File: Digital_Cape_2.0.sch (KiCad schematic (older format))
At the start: 15 parts, among them J1 RJ45, J2 RJ45, P8 BeagleBone_Black_Header, P9 BeagleBone_Black_Header

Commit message: Update of KiCad files
My apologies I'm still learning! Files from 02-13-2021 Hangar session
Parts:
- added H1, H2, H3, H4: MountingHole, MountingHole:MountingHole_3.2mm_M3, symbol Mechanical:MountingHole
- added R1, R2: 4.7k, Resistor_THT:R_Axial_DIN0204_L3.6mm_D1.6mm_P5.08mm_Horizontal, symbol Device:R
- C1, C2, C3, C4, C5, CP1, CP2: footprint Capacitor_SMD:CP_Elec_4x4.5 -> Capacitor_THT:C_Disc_D3.0mm_W2.0mm_P2.50mm
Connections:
- net labels removed: GND1, GND2, GNDA_ADC, GNDD
- wire segments 139 -> 164
- no-connect marks 78 -> 76

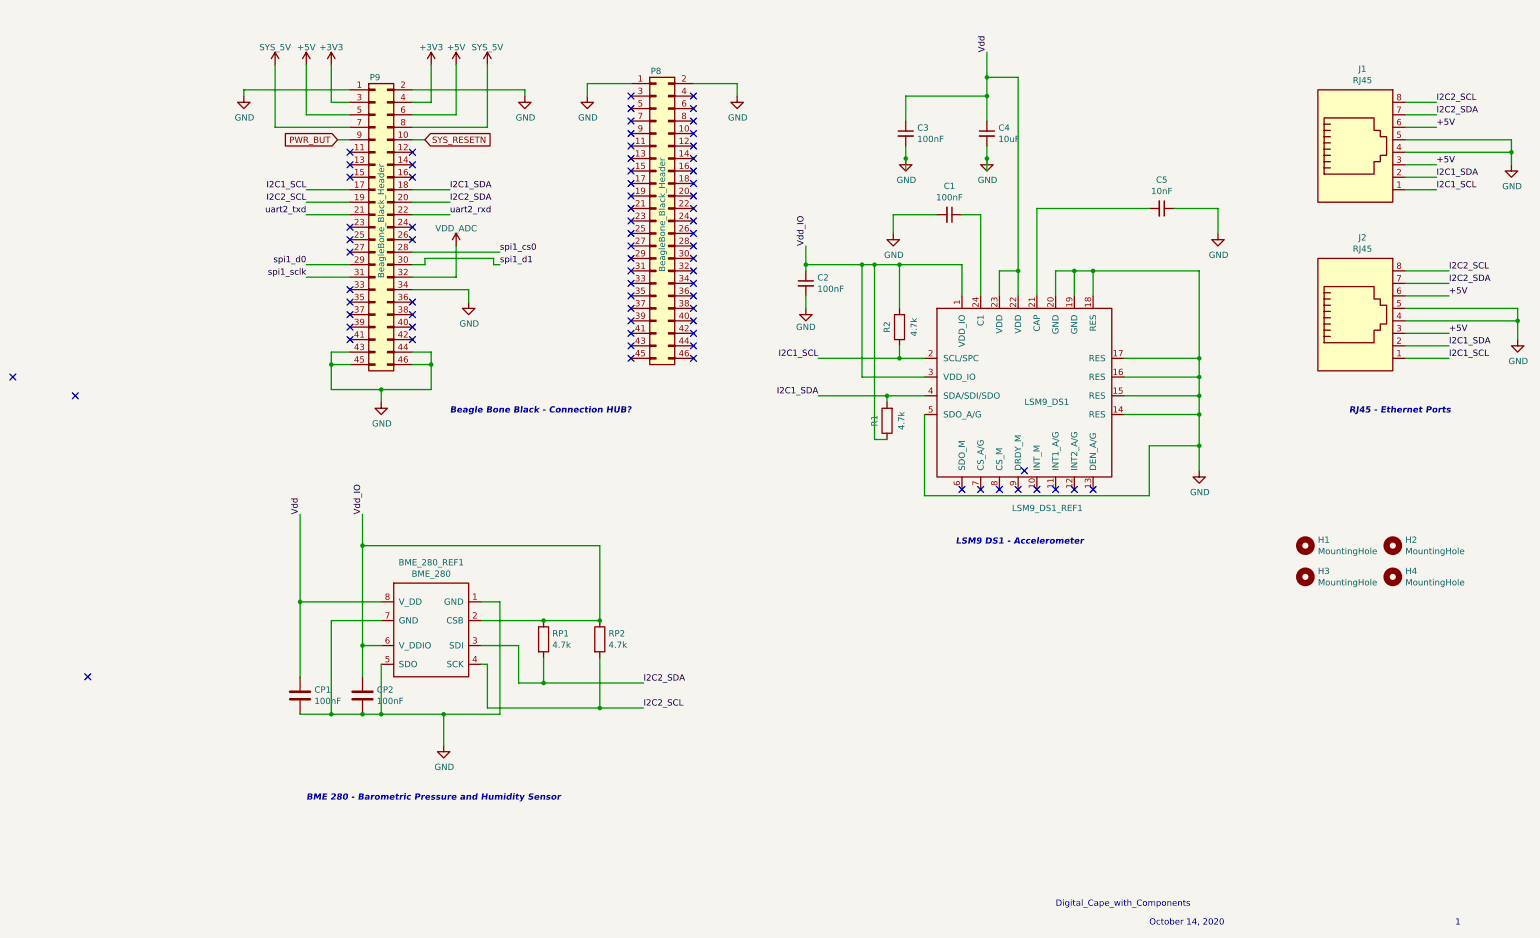
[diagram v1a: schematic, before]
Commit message: Update board to fit BBB cape spec
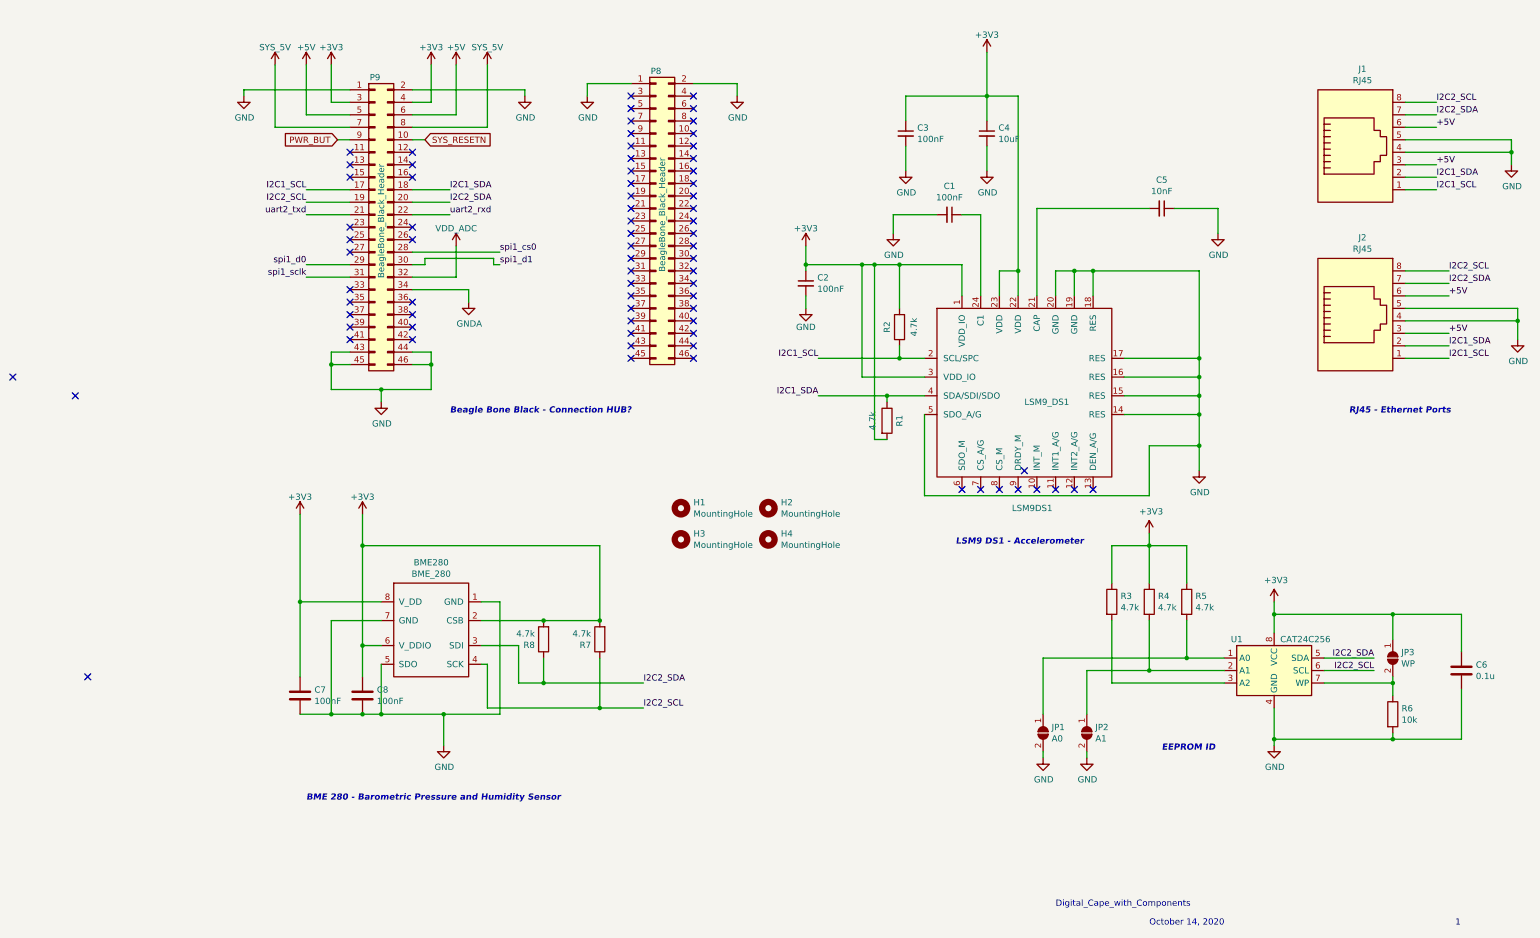
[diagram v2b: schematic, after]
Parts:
- added C6: 0.1u, Capacitor_THT:C_Disc_D3.0mm_W2.0mm_P2.50mm, symbol Device:C
- added JP1: A0, Jumper:SolderJumper-2_P1.3mm_Open_Pad1.0x1.5mm, symbol Jumper:SolderJumper_2_Open
- added JP2: A1, Jumper:SolderJumper-2_P1.3mm_Open_Pad1.0x1.5mm, symbol Jumper:SolderJumper_2_Open
- added JP3: WP, Jumper:SolderJumper-2_P1.3mm_Open_Pad1.0x1.5mm, symbol Jumper:SolderJumper_2_Open
- added R3, R4, R5: 4.7k, Resistor_THT:R_Axial_DIN0204_L3.6mm_D1.6mm_P5.08mm_Horizontal, symbol Device:R
- added R6: 10k, Resistor_THT:R_Axial_DIN0204_L3.6mm_D1.6mm_P5.08mm_Horizontal, symbol Device:R
- added U1: CAT24C256, Package_SO:SOIC-8_3.9x4.9mm_P1.27mm, symbol Memory_EEPROM:CAT24C256
- H1, H2, H3, H4: footprint MountingHole:MountingHole_3.2mm_M3 -> MountingHole:MountingHole_3mm
- renumbered BME_280_REF1 to BME280, CP1 to C7, CP2 to C8, LSM9_DS1_REF1 to LSM9DS1, RP1 to R7, RP2 to R8
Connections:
- net Vdd is gone; now on net +3V3: BME280.8 (V_DD), C3.1, C4.1, C7.1, LSM9DS1.22 (VDD), LSM9DS1.23 (VDD)
- net +3V3: now also BME280.2 (CSB), BME280.6 (V_DDIO), C2.1, C8.1, LSM9DS1.1 (VDD_IO), LSM9DS1.3 (VDD_IO), R1.2, R2.2, R7.2, R8.2, C6.1, JP3.1 (A), R3.1, R4.1, R5.1, U1.8 (VCC)
- net GND: now also C6.2, JP1.2 (B), JP2.2 (B), R6.2, U1.4 (GND); no longer P9.34 (Pin_34)
- net I2C1_SDA: now also R1.1; no longer R1.2
- net I2C2_SCL: now also R7.1, U1.6 (SCL); no longer R8.2
- net I2C2_SDA: now also R8.1, U1.5 (SDA); no longer R7.2
- removed net Vdd_IO: BME280.2 (CSB), BME280.6 (V_DDIO), C2.1, C8.1, LSM9DS1.1 (VDD_IO), LSM9DS1.3 (VDD_IO), R1.1, R2.2, R7.1, R8.1
- new net: JP1.1 (A), R5.2, U1.1 (A0)
- new net: JP2.1 (A), R4.2, U1.2 (A1)
- new net: R3.2, U1.3 (A2)
- new net: JP3.2 (B), R6.1, U1.7 (WP)
- new net GNDA: P9.34 (Pin_34)
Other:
- note added: "EEPROM ID"
- moved on the sheet: H1, H2, H3, H4, R7, R8

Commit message: Switch BME to use standard library component
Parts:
- BME280: symbol Digital_Cape_2.0-rescue:BME_280-BME_280_Baro_Pressure -> Sensor:BME280
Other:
- moved on the sheet: C7, C8, R7, R8
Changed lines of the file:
@@
 I2C2_SCL
 $Comp
-L Digital_Cape_2.0-rescue:BME_280-BME_280_Baro_Pressure BME280
+L Sensor:BME280 BME280
 U 1 1 5F9DE29A
-P 2350 5450
-F 0 "BME280" H 2350 6165 50  0000 C CNN
-F 1 "BME_280" H 2350 6074 50  0000 C CNN
-F 2 "Package_LGA:Bosch_LGA-8_2.5x2.5mm_P0.65mm_ClockwisePinNumbering" H 1800 6150 50  0001 C CNN
-F 3 "" H 1800 6150 50  0001 C CNN
-	1    2350 5450
-	1    0    0    -1
-$EndComp
-$Comp
-L power:GND #PWR0107
-U 1 1 5F9DF982
-P 2450 6200
-F 0 "#PWR0107" H 2450 5950 50  0001 C CNN
-F 1 "GND" H 2455 6027 50  0000 C CNN
-F 2 "" H 2450 6200 50  0001 C CNN
-F 3 "" H 2450 6200 50  0001 C CNN
-	1    2450 6200
+P 2500 5400
+F 0 "BME280" H 2800 5850 50  0000 C CNN
+F 1 "BME_280" H 2150 5850 50  0000 C CNN
+F 2 "Package_LGA:Bosch_LGA-8_2.5x2.5mm_P0.65mm_ClockwisePinNumbering" H 1950 6100 50  0001 C CNN
+F 3 "" H 1950 6100 50  0001 C CNN
+	1    2500 5400
 	1    0    0    -1
 $EndComp
@@
 L Device:C C8
 U 1 1 5F9E0803
-P 1800 5800
-F 0 "C8" H 1915 5846 50  0000 L CNN
-F 1 "100nF" H 1915 5755 50  0000 L CNN
-F 2 "Capacitor_THT:C_Disc_D3.0mm_W2.0mm_P2.50mm" H 1838 5650 50  0001 C CNN
-F 3 "~" H 1800 5800 50  0001 C CNN
-	1    1800 5800
+P 1650 5400
+F 0 "C8" H 1765 5446 50  0000 L CNN
+F 1 "100nF" H 1765 5355 50  0000 L CNN
+F 2 "Capacitor_THT:C_Disc_D3.0mm_W2.0mm_P2.50mm" H 1688 5250 50  0001 C CNN
+F 3 "~" H 1650 5400 50  0001 C CNN
+	1    1650 5400
 	1    0    0    -1
 $EndComp
@@
 L Device:C C7
 U 1 1 5F9E108B
-P 1300 5800
-F 0 "C7" H 1415 5846 50  0000 L CNN
-F 1 "100nF" H 1415 5755 50  0000 L CNN
-F 2 "Capacitor_THT:C_Disc_D3.0mm_W2.0mm_P2.50mm" H 1338 5650 50  0001 C CNN
-F 3 "~" H 1300 5800 50  0001 C CNN
-	1    1300 5800
-	1    0    0    -1
-$EndComp
-$Comp
-L Device:R R7
-U 1 1 5F9E1AD3
-P 3700 5350
-F 0 "R7" H 3770 5396 50  0000 L CNN
-F 1 "4.7k" H 3770 5305 50  0000 L CNN
-F 2 "Resistor_THT:R_Axial_DIN0204_L3.6mm_D1.6mm_P5.08mm_Horizontal" V 3630 5350 50  0001 C CNN
-F 3 "~" H 3700 5350 50  0001 C CNN
-	1    3700 5350
-	-1   0    0    1
-$EndComp
-$Comp
-L Device:R R8
-U 1 1 5F9E2971
-P 3250 5350
-F 0 "R8" H 3320 5396 50  0000 L CNN
-F 1 "4.7k" H 3320 5305 50  0000 L CNN
-F 2 "Resistor_THT:R_Axial_DIN0204_L3.6mm_D1.6mm_P5.08mm_Horizontal" V 3180 5350 50  0001 C CNN
-F 3 "~" H 3250 5350 50  0001 C CNN
-	1    3250 5350
-	-1   0    0    1
-$EndComp
-Wire Wire Line
-	2750 5050 2900 5050
-Wire Wire Line
-	1950 5400 1800 5400
-Wire Wire Line
-	1800 5400 1800 4600
-Wire Wire Line
-	1800 5400 1800 5650
-Connection ~ 1800 5400
-Wire Wire Line
-	2900 5950 2450 5950
-Wire Wire Line
-	2450 5950 2450 6200
-Wire Wire Line
-	2900 5050 2900 5950
-Wire Wire Line
-	1800 5950 1950 5950
-Connection ~ 2450 5950
-Wire Wire Line
-	1300 5950 1550 5950
-Connection ~ 1800 5950
-Wire Wire Line
-	1300 5650 1300 5050
-Wire Wire Line
-	1950 5200 1550 5200
-Wire Wire Line
-	1550 5200 1550 5950
-Connection ~ 1550 5950
-Wire Wire Line
-	1550 5950 1800 5950
-Wire Wire Line
-	1950 5050 1300 5050
-Connection ~ 1300 5050
-Wire Wire Line
-	1300 5050 1300 4350
-Wire Wire Line
-	2750 5200 3250 5200
-Wire Wire Line
-	3250 5200 3700 5200
-Connection ~ 3250 5200
-Wire Wire Line
-	3700 5200 3700 4600
-Wire Wire Line
-	3700 4600 1800 4600
-Connection ~ 3700 5200
-Connection ~ 1800 4600
-Wire Wire Line
-	1800 4600 1800 4350
-Wire Wire Line
-	2750 5550 2800 5550
-Wire Wire Line
-	2800 5550 2800 5900
-Wire Wire Line
-	2800 5900 3700 5900
-Wire Wire Line
-	2750 5400 3050 5400
-Wire Wire Line
-	3050 5400 3050 5700
-Wire Wire Line
-	3050 5700 3250 5700
-Wire Wire Line
-	3250 5500 3250 5700
-Connection ~ 3250 5700
-Wire Wire Line
-	3250 5700 4050 5700
-Wire Wire Line
-	3700 5500 3700 5900
-Connection ~ 3700 5900
-Wire Wire Line
-	3700 5900 4050 5900
+P 1150 5400
+F 0 "C7" H 1265 5446 50  0000 L CNN
+F 1 "100nF" H 1265 5355 50  0000 L CNN
+F 2 "Capacitor_THT:C_Disc_D3.0mm_W2.0mm_P2.50mm" H 1188 5250 50  0001 C CNN
+F 3 "~" H 1150 5400 50  0001 C CNN
+	1    1150 5400
+	1    0    0    -1
+$EndComp
 Text Notes 1350 6650 0    50   Italic 10
 BME 280 - Barometric Pressure and Humidity Sensor
@@
 Text Label 5450 3400 2    50   ~ 0
 I2C1_SDA
-Text Label 4050 5700 0    50   ~ 0
+Text Label 4100 5500 2    50   ~ 0
 I2C2_SDA
-Text Label 4050 5900 0    50   ~ 0
+Text Label 4100 5300 2    50   ~ 0
 I2C2_SCL
 NoConn ~ 3950 1000
@@
 Wire Wire Line
 	8500 3800 8500 4000
-Wire Wire Line
-	1950 5550 1950 5950
-Connection ~ 1950 5950
-Wire Wire Line
-	1950 5950 2450 5950
 $Comp
 L Mechanical:MountingHole H1
@@
 	6800 1400 6800 1600
 $Comp
-L power:+3.3V #PWR?
+L power:+3.3V #PWR0107
 U 1 1 605027B5
 P 6800 650
-F 0 "#PWR?" H 6800 500 50  0001 C CNN
+F 0 "#PWR0107" H 6800 500 50  0001 C CNN
 F 1 "+3V3" H 6800 790 50  0000 C CNN
 F 2 "" H 6800 650 60  0000 C CNN
@@
 $EndComp
 $Comp
-L power:+3.3V #PWR?
+L power:+3.3V #PWR0111
 U 1 1 6050881B
 P 5350 2200
-F 0 "#PWR?" H 5350 2050 50  0001 C CNN
+F 0 "#PWR0111" H 5350 2050 50  0001 C CNN
 F 1 "+3V3" H 5350 2340 50  0000 C CNN
 F 2 "" H 5350 2200 60  0000 C CNN
@@
 $EndComp
 $Comp
-L power:+3.3V #PWR?
-U 1 1 6051FCC3
-P 1300 4350
-F 0 "#PWR?" H 1300 4200 50  0001 C CNN
-F 1 "+3V3" H 1300 4490 50  0000 C CNN
-F 2 "" H 1300 4350 60  0000 C CNN
-F 3 "" H 1300 4350 60  0000 C CNN
-	1    1300 4350
-	1    0    0    -1
-$EndComp
-$Comp
-L power:+3.3V #PWR?
-U 1 1 60520721
-P 1800 4350
-F 0 "#PWR?" H 1800 4200 50  0001 C CNN
-F 1 "+3V3" H 1800 4490 50  0000 C CNN
-F 2 "" H 1800 4350 60  0000 C CNN
-F 3 "" H 1800 4350 60  0000 C CNN
-	1    1800 4350
-	1    0    0    -1
-$EndComp
+L Device:R R8
+U 1 1 5F9E2971
+P 3650 4850
+F 0 "R8" H 3720 4896 50  0000 L CNN
+F 1 "4.7k" H 3720 4805 50  0000 L CNN
+F 2 "Resistor_THT:R_Axial_DIN0204_L3.6mm_D1.6mm_P5.08mm_Horizontal" V 3580 4850 50  0001 C CNN
+F 3 "~" H 3650 4850 50  0001 C CNN
+	1    3650 4850
+	-1   0    0    1
+$EndComp
+Wire Wire Line
+	2400 4800 2400 4600
+$Comp
+L power:+3V3 #PWR0116
+U 1 1 6057A403
+P 2500 4500
+F 0 "#PWR0116" H 2500 4350 50  0001 C CNN
+F 1 "+3V3" H 2515 4673 50  0000 C CNN
+F 2 "" H 2500 4500 50  0001 C CNN
+F 3 "" H 2500 4500 50  0001 C CNN
+	1    2500 4500
+	1    0    0    -1
+$EndComp
+Wire Wire Line
+	2500 4500 2500 4600
+Wire Wire Line
+	2500 4600 2400 4600
+Wire Wire Line
+	2500 4600 2600 4600
+Wire Wire Line
+	2600 4600 2600 4800
+Connection ~ 2500 4600
+Wire Wire Line
+	2400 6000 2400 6200
+Wire Wire Line
+	2400 6200 2500 6200
+Wire Wire Line
+	2500 6200 2500 6250
+Connection ~ 2500 6200
+Wire Wire Line
+	2500 6200 2600 6200
+$Comp
+L power:GND #PWR0117
+U 1 1 605AF79D
+P 2500 6250
+F 0 "#PWR0117" H 2500 6000 50  0001 C CNN
+F 1 "GND" H 2505 6077 50  0000 C CNN
+F 2 "" H 2500 6250 50  0001 C CNN
+F 3 "" H 2500 6250 50  0001 C CNN
+	1    2500 6250
+	1    0    0    -1
+$EndComp
+$Comp
+L Device:R R7
+U 1 1 5F9E1AD3
+P 3300 4850
+F 0 "R7" H 3370 4896 50  0000 L CNN
+F 1 "4.7k" H 3370 4805 50  0000 L CNN
+F 2 "Resistor_THT:R_Axial_DIN0204_L3.6mm_D1.6mm_P5.08mm_Horizontal" V 3230 4850 50  0001 C CNN
+F 3 "~" H 3300 4850 50  0001 C CNN
+	1    3300 4850
+	-1   0    0    1
+$EndComp
+Wire Wire Line
+	3100 5500 3650 5500
+Wire Wire Line
+	3100 5300 3300 5300
+Wire Wire Line
+	3300 5300 3300 5000
+Wire Wire Line
+	3100 5100 3250 5100
+Wire Wire Line
+	3250 5100 3250 6200
+Wire Wire Line
+	3250 6200 2600 6200
+Connection ~ 2600 6200
+Wire Wire Line
+	2600 6200 2600 6000
+Wire Wire Line
+	3650 5000 3650 5500
+Wire Wire Line
+	3300 4700 3300 4600
+Wire Wire Line
+	3300 4600 2600 4600
+Connection ~ 2600 4600
+Wire Wire Line
+	3650 4700 3650 4600
+Wire Wire Line
+	3650 4600 3400 4600
+Connection ~ 3300 4600
+Wire Wire Line
+	3100 5700 3400 5700
+Wire Wire Line
+	3400 5700 3400 4600
+Connection ~ 3400 4600
+Wire Wire Line
+	3400 4600 3300 4600
+Wire Wire Line
+	2400 4600 1650 4600
+Wire Wire Line
+	1650 4600 1650 5250
+Connection ~ 2400 4600
+Wire Wire Line
+	1150 5250 1150 4600
+Wire Wire Line
+	1150 4600 1650 4600
+Connection ~ 1650 4600
+Wire Wire Line
+	1650 5550 1650 6200
+Wire Wire Line
+	1650 6200 2400 6200
+Connection ~ 2400 6200
+Wire Wire Line
+	1150 5550 1150 6200
+Wire Wire Line
+	1150 6200 1650 6200
+Connection ~ 1650 6200
+Wire Wire Line
+	4100 5500 3650 5500
+Connection ~ 3650 5500
+Wire Wire Line
+	3300 5300 4100 5300
+Connection ~ 3300 5300
 $EndSCHEMATC

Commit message: Fix LSM9DS1
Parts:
- U3: renamed from LSM9DS1; symbol Digital_Cape_2.0-rescue:LSM9_DS1-LSM9_DS1_Accelerometer -> Sensor_Motion:LSM9DS1
- renumbered BME280 to U2
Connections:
- net +3V3: now also U3.7 (CS_A/G), U3.8 (CS_M)
- net GND: now also C5.2, U3.6 (SDO_M); no longer C5.1
- net LSM9_EN: now reaches P9.33 (Pin_33)
- net LSM9_EN: now also U3.13 (DEN_A/G)
- net INT2_A: now reaches P9.35 (Pin_35)
- net INT2_A: now also U3.12 (INT2_A/G)
- net INT1_A: now reaches P9.37 (Pin_37)
- net INT1_A: now also U3.11 (INT1_A/G)
- net DRDY_M: now reaches P9.39 (Pin_39)
- net DRDY_M: now also U3.10 (INT_M)
- net INT_M: now reaches P9.41 (Pin_41)
- net INT_M: now also U3.9 (DRDY_M)
- net at U3.21 (CAP): now also C5.1; no longer C5.2
- no-connect marks 76 -> 62
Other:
- moved on the sheet: C1, C2, C3, C4, C5, R1, R2

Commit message: Switch pin headers to default libs
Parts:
- P8, P9: footprint Socket_BeagleBone_Black:Socket_BeagleBone_Black -> Connector_PinHeader_2.54mm:PinHeader_2x23_P2.54mm_Vertical
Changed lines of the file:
@@
 F 0 "P8" H 4150 3200 50  0000 C CNN
 F 1 "BeagleBone_Black_Header" V 4200 2050 50  0000 C CNN
-F 2 "Socket_BeagleBone_Black:Socket_BeagleBone_Black" H 4150 1150 60  0001 C CNN
+F 2 "Connector_PinHeader_2.54mm:PinHeader_2x23_P2.54mm_Vertical" H 4150 1150 60  0001 C CNN
 F 3 "" H 4150 1150 60  0000 C CNN
 	1    4150 2000
@@
 F 0 "P9" H 1900 3250 50  0000 C CNN
 F 1 "BeagleBone_Black_Header" V 1950 2100 50  0000 C CNN
-F 2 "Socket_BeagleBone_Black:Socket_BeagleBone_Black" H 1900 1200 60  0001 C CNN
+F 2 "Connector_PinHeader_2.54mm:PinHeader_2x23_P2.54mm_Vertical" H 1900 1200 60  0001 C CNN
 F 3 "" H 1900 1200 60  0000 C CNN
 	1    1900 2050

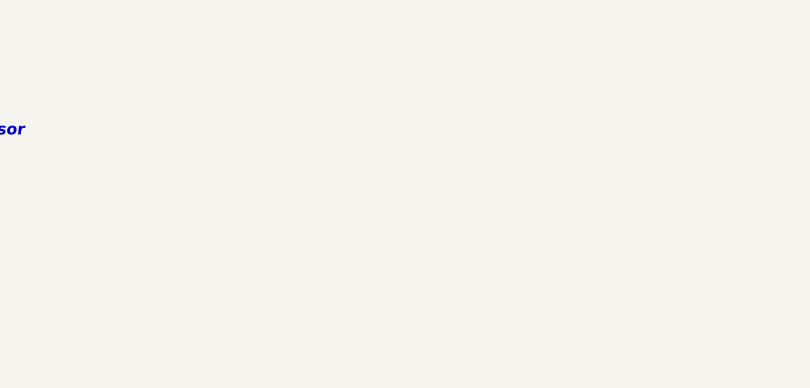
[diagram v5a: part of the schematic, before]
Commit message: Add power flags
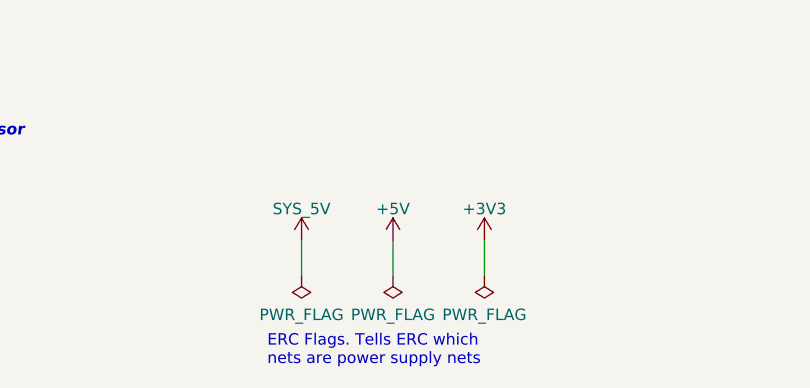
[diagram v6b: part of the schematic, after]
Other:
- note added: "ERC Flags. Tells ERC which \nnets are power supply nets\n"
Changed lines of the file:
@@
 NoConn ~ 2200 2850
 NoConn ~ 2200 2950
+$Comp
+L power:PWR_FLAG #FLG0101
+U 1 1 60DA570A
+P 4600 7250
+F 0 "#FLG0101" H 4600 7325 50  0001 C CNN
+F 1 "PWR_FLAG" H 4600 7423 50  0000 C CNN
+F 2 "" H 4600 7250 50  0001 C CNN
+F 3 "~" H 4600 7250 50  0001 C CNN
+	1    4600 7250
+	-1   0    0    1
+$EndComp
+$Comp
+L power:+3.3V #PWR0106
+U 1 1 60DAF410
+P 5400 7100
+F 0 "#PWR0106" H 5400 6950 50  0001 C CNN
+F 1 "+3V3" H 5400 7240 50  0000 C CNN
+F 2 "" H 5400 7100 60  0000 C CNN
+F 3 "" H 5400 7100 60  0000 C CNN
+	1    5400 7100
+	1    0    0    -1
+$EndComp
+$Comp
+L power:+5V #PWR0107
+U 1 1 60DAF866
+P 5000 7100
+F 0 "#PWR0107" H 5000 6950 50  0001 C CNN
+F 1 "+5V" H 5000 7240 50  0000 C CNN
+F 2 "" H 5000 7100 60  0000 C CNN
+F 3 "" H 5000 7100 60  0000 C CNN
+	1    5000 7100
+	1    0    0    -1
+$EndComp
+$Comp
+L pwr_BeagleBone:SYS_5V #PWR0118
+U 1 1 60DAF870
+P 4600 7100
+F 0 "#PWR0118" H 4600 6950 50  0001 C CNN
+F 1 "SYS_5V" H 4600 7240 50  0000 C CNN
+F 2 "" H 4600 7100 60  0000 C CNN
+F 3 "" H 4600 7100 60  0000 C CNN
+	1    4600 7100
+	1    0    0    -1
+$EndComp
+$Comp
+L power:PWR_FLAG #FLG0102
+U 1 1 60DC27F2
+P 5000 7250
+F 0 "#FLG0102" H 5000 7325 50  0001 C CNN
+F 1 "PWR_FLAG" H 5000 7423 50  0000 C CNN
+F 2 "" H 5000 7250 50  0001 C CNN
+F 3 "~" H 5000 7250 50  0001 C CNN
+	1    5000 7250
+	-1   0    0    1
+$EndComp
+$Comp
+L power:PWR_FLAG #FLG0103
+U 1 1 60DC2A69
+P 5400 7250
+F 0 "#FLG0103" H 5400 7325 50  0001 C CNN
+F 1 "PWR_FLAG" H 5400 7423 50  0000 C CNN
+F 2 "" H 5400 7250 50  0001 C CNN
+F 3 "~" H 5400 7250 50  0001 C CNN
+	1    5400 7250
+	-1   0    0    1
+$EndComp
+Wire Wire Line
+	5400 7100 5400 7250
+Wire Wire Line
+	5000 7250 5000 7100
+Wire Wire Line
+	4600 7100 4600 7250
+Text Notes 4450 7650 0    50   ~ 0
+ERC Flags. Tells ERC which \nnets are power supply nets\n
 $EndSCHEMATC
